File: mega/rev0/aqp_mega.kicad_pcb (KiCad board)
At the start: 2 copper layers, 313 x 326.6 mm, 174 parts, among them J1 Power in, J10 FPGA spare, J11 Hand controller 2, J12 Hand controller 1, J13 ESP32 spare, J2 ESP USB Host, J3 Audio out, J4 VGA, J5 Cassette out, J6 Cassette in, J7 Expansion port, J8 Printer, J9 TF-03A, Q1 BC847C, Q2 BC847C, Q3 2N7002, SW1 SW_DPDT_x2, U1 SN74AHCT1G125DBVR, U10 ESP32-S3-WROOM-1-N4R2, U11 LDL1117S33R, U12 SN74CB3T3245PWR, U13 IS61C5128AS-25QLI, U2 SN74AHCT1G125DBVR, U3 LD1117S12, U4 SN74CB3T3245PWR, U5 MAX3221ECPWR, U6 XC6SLX9-2TQG144C, U7 Z84C3008VEG, U8 SN74CB3T3245PWR, U9 SN74CB3T3245PWR, X1 SX3M14.31818M20F30TNN

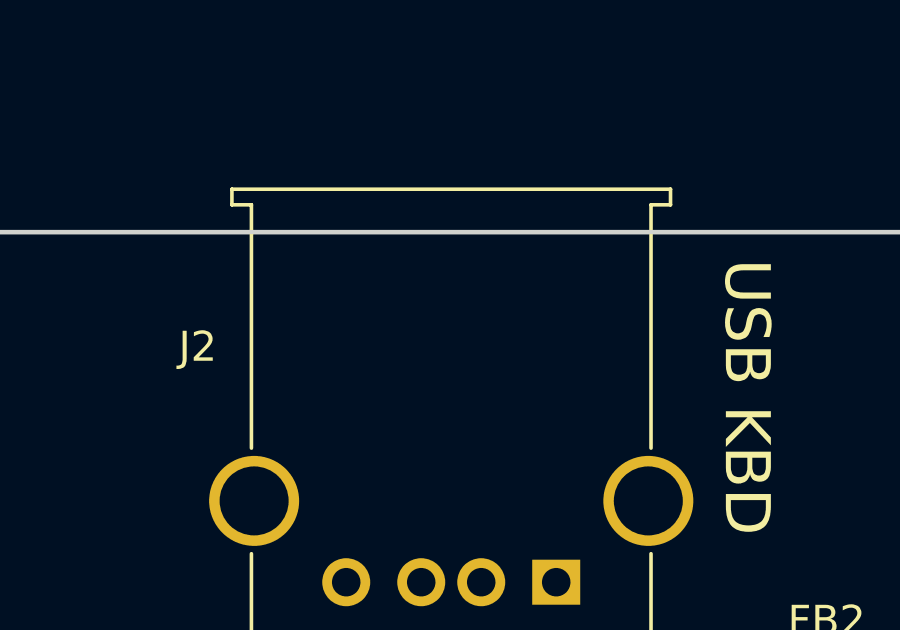
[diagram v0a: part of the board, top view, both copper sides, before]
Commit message: PCB folder updates and reorg
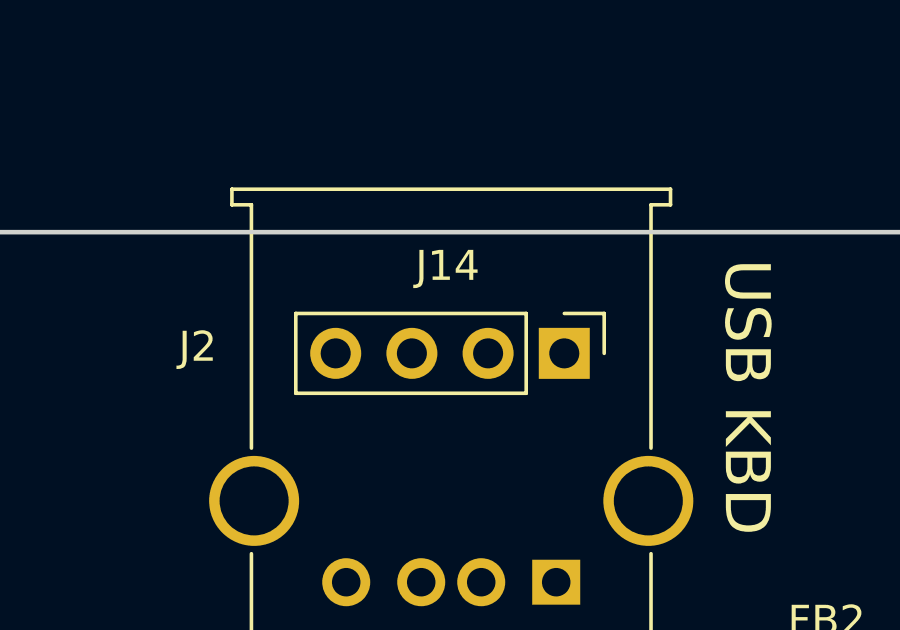
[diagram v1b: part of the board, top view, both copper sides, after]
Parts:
- added J14: Conn_01x04, Connector_PinHeader_2.54mm:PinHeader_1x04_P2.54mm_Vertical, F.Cu at (238.4, 72.8)
